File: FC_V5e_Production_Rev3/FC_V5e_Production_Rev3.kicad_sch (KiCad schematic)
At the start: 72 parts, among them IC3 RV-3028-C7_32.768kHz_1ppm_TA_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, J12 USB_C_Receptacle_USB2.0_16P, J16 DEBUG, J18 Payload, J22 SWD Port, J3 Life Makes Lemonade, J5 BM04B-SRSS-TB(LF)(SN), SW1 KMR2, SW2 KMR2, U13 E22-400M30S, U15 LIS2MDL, U2 ZDSD02GLGEAG, U3 TCA9548APWR, U30 E28-2G4M27S, U7 LSM6DSOTR

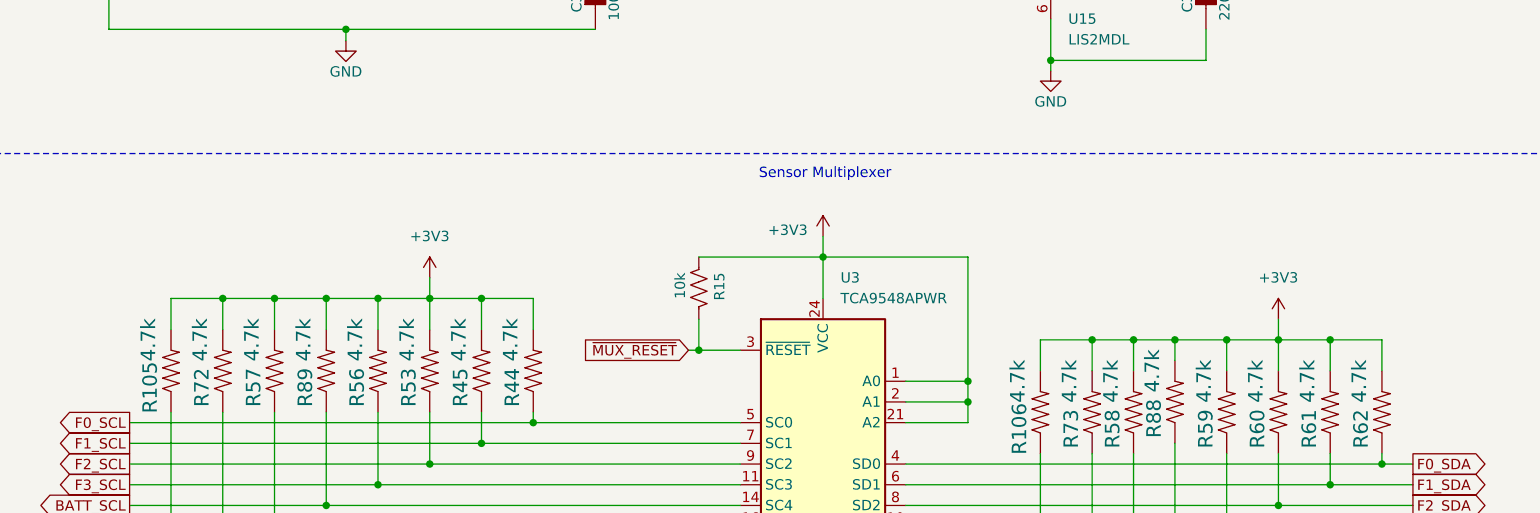
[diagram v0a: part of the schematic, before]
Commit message: V5e_Rev3: Face I2C pull-ups on the switched face rail
Each face channel's 4.7k SDA/SCL pull-ups (R44/R62, R45/R61, R53/R60,
R56/R59, R57/R58, R72/R73) now return to that face's Fx_PWR instead of
always-on +3V3, so an unpowered face (the bufferless XY_Face_V4nb, whose
DRV2605L clamps SDA/SCL to VDD) is not back-powered through them.

Schematic: pin 2 of the 12 resistors moves from the +3V3 bus to Fx_PWR
global labels; R105/R106/R88/R89 and the mux upstream pull-ups stay on
+3V3. Netlist diff is exactly those 12 pins.

PCB: the pairs leave the B.Cu cluster at the TCA9548A and sit next to
their face connector where Fx_SDA/SCL/PWR already run. F0, F4 need no
new vias; F1, F2, F5 add short vias to reach Fx_PWR or the signal on the
other layer; F3 stays on B.Cu below U24. Dead pull-up stubs and vias at
the mux and the +3V3 vias at the old F4 pair are removed. Zones refilled
(zone fill data churns). DRC/parity identical to baseline: 39 violations,
0 unconnected, 14 parity, all pre-existing.

Co-Authored-By: Claude Opus 5.5 (1M context) <noreply@anthropic.com>
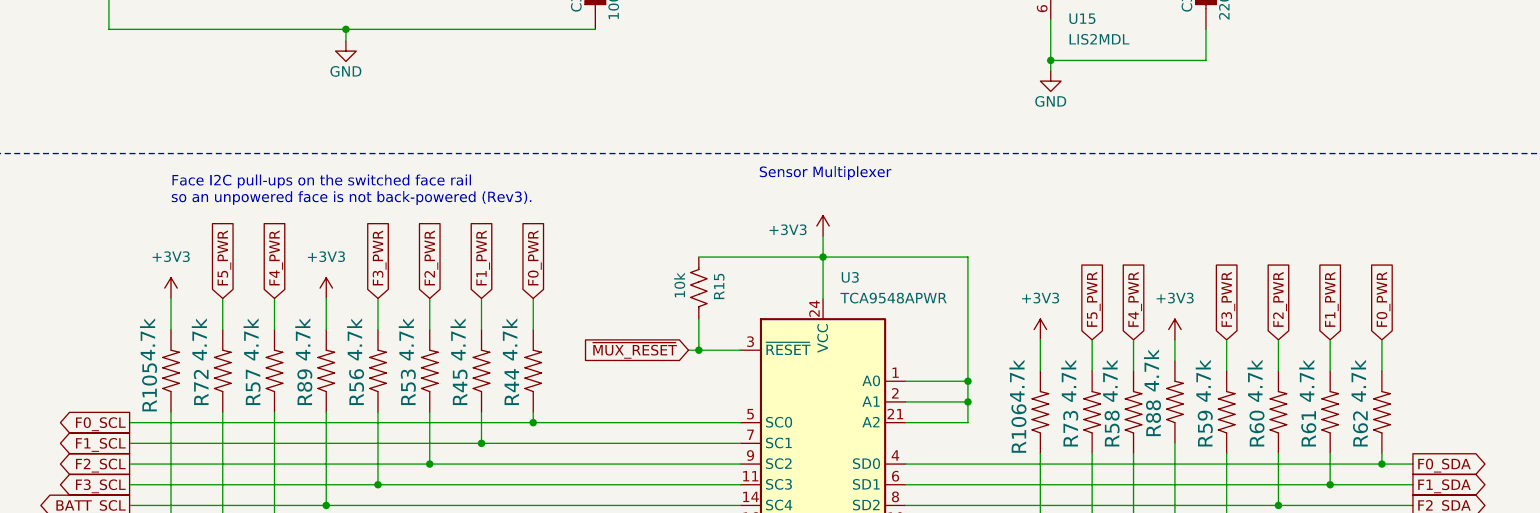
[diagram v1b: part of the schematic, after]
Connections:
- net +3V3: no longer R44.2, R45.2, R53.2, R56.2, R57.2, R58.2, R59.2, R60.2, R61.2, R62.2, R72.2, R73.2
- new net F0_PWR: R44.2, R62.2
- new net F1_PWR: R45.2, R61.2
- new net F2_PWR: R53.2, R60.2
- new net F3_PWR: R56.2, R59.2
- new net F4_PWR: R57.2, R58.2
- new net F5_PWR: R72.2, R73.2
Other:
- note added: "Face I2C pull-ups on the switched face rail so an unpowered face is not back-powered (Rev3)."

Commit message: V5e_Rev3: Face pull-up layout review fixes and mux firmware note
- R57: move the F4_SCL via out from under pad 1 to (219.45, 88.60) and
  re-stub on F.Cu. Ring now clears the pad by 0.24 mm (was overlapping).
- R60: move the F2_PWR via to (220.10, 114.33). Ring to pad 2 edge is
  0.20 mm (was 0.05 mm).
- F0_SCL: R44 pad 1 now lands on the trunk with a 45-degree leg plus a
  vertical, removing the 65-degree acute junction.
- R56: shift 0.2 mm toward -x. Courtyard gap to J13 is 0.175 mm (was 0.04 mm).
- Main sheet: add the TCA9548A channel-select rule under the pull-up bank
  and a short pointer next to U3.

Netlist unchanged; DRC and ERC results identical to aa824d3.

Co-Authored-By: Claude Opus 5.5 (1M context) <noreply@anthropic.com>
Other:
- note added: "Do not select a TCA9548A channel whose face is off (bus parks mid-rail). Deselect the channel before FACEx_ENABLE=0; select only after the face rail is up (>150 us). ~MUX_RESET (GPIO26) recovers a parked bus."
- note added: "Firmware: never select an unpowered face channel; see pull-up note."
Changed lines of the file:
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@@
+		)
+	)
+	(text "Do not select a TCA9548A channel whose face is off\n(bus parks mid-rail). Deselect the channel before\nFACEx_ENABLE=0; select only after the face rail is up\n(>150 us). ~MUX_RESET (GPIO26) recovers a parked bus."
+		(exclude_from_sim no)
+		(at 233.68 142.24 0)
+		(effects
+			(font
+				(size 1.27 1.27)
+			)
+			(justify left top)
+		)
+	)
+	(text "Firmware: never select an unpowered\nface channel; see pull-up note."
+		(exclude_from_sim no)
+		(at 325.12 147.32 0)
+		(effects
+			(font
+				(size 1.27 1.27)
+			)
+			(justify left top)
 		)
 	)

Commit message: V5e_Rev3: Clear F1/F5 PWR vias off load-switch pins; reword mux note
- F5_PWR via (219.60,92.40) -> (219.85,92.40), along its own B.Cu
  U27.6 -> J2.4 trace. Ring gap to U27.6 0.050 -> 0.30 mm.
- F1_PWR via (219.80,108.25) -> (220.11,108.03), B.Cu stub to the
  U21.6 -> J9.4 trace. Ring gap to U21.6 0.070 -> 0.234 mm.
- R59 +0.1 mm in y. R56/R59 courtyard gap 0.07 -> 0.17 mm.
- Mux bank note: select a channel only after the face rail has
  settled (AP22653 soft-start) plus the 150 us TCA4311A idle time.

Netlist, ERC (460) and DRC multisets match 513008e.

Co-Authored-By: Claude Opus 5.5 (1M context) <noreply@anthropic.com>
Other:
- note added: "Do not select a TCA9548A channel whose face is off (bus parks mid-rail). Deselect the channel before FACEx_ENABLE=0; select only after the face rail has settled (AP22653 soft-start) plus 150 us TCA4311A idle time. ~MUX_RESET (GPIO26) recovers a parked bus."
- note removed: "Do not select a TCA9548A channel whose face is off (bus parks mid-rail). Deselect the channel before FACEx_ENABLE=0; select only after the face rail is up (>150 us). ~MUX_RESET (GPIO26) recovers a parked bus."
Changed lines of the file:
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@@
 		)
 	)
-	(text "Do not select a TCA9548A channel whose face is off\n(bus parks mid-rail). Deselect the channel before\nFACEx_ENABLE=0; select only after the face rail is up\n(>150 us). ~MUX_RESET (GPIO26) recovers a parked bus."
+	(text "Do not select a TCA9548A channel whose face is off\n(bus parks mid-rail). Deselect the channel before\nFACEx_ENABLE=0; select only after the face rail has settled\n(AP22653 soft-start) plus 150 us TCA4311A idle time.\n~MUX_RESET (GPIO26) recovers a parked bus."
 		(exclude_from_sim no)
 		(at 233.68 142.24 0)
